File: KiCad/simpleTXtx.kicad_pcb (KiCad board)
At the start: 2 copper layers, 18 x 30 mm, 13 parts, among them J1 BAT, J2 VIDEO, Q1 2SC1815

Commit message: update project
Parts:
- removed J1: BAT, Connector_PinHeader_2.54mm:PinHeader_1x02_P2.54mm_Vertical
- added J3: RCJ-044, RCJ-044:CUI_RCJ-044, F.Cu at (157.0, 85.0)
- C3, C4: footprint Capacitor_THT:C_Disc_D4.3mm_W1.9mm_P5.00mm -> Capacitor_THT:C_Disc_D11.0mm_W5.0mm_P5.00mm
- J2: value VIDEO -> Barrel_Jack_MountingPin; footprint Connector_PinHeader_2.54mm:PinHeader_1x02_P2.54mm_Vertical -> Connector_BarrelJack:BarrelJack_GCT_DCJ200-10-A_Horizontal
- RV1: footprint Potentiometer_THT:Potentiometer_Bourns_3266Y_Vertical -> Potentiometer_THT:Potentiometer_Runtron_RM-065_Vertical
- moved J2 22.1 mm to (138.5, 75.7), turned to 0 degrees
- moved C5 19.9 mm to (155.0, 59.0)
- moved RV1 18.1 mm to (134.5, 59.5)
- moved C4 16.4 mm to (136.0, 69.5), turned to 0 degrees
- moved L1 13.0 mm to (148.0, 79.7), turned to -90 degrees
- moved C3 4.41 mm to (148.0, 68.4), turned to -90 degrees
- moved AE1 4.01 mm to (147.0, 60.5)
- moved C2 2.28 mm to (157.0, 70.5)
- moved R1 2.16 mm to (160.5, 67.5)
- moved C1 2.14 mm to (160.5, 70.5)
- moved R2 1.19 mm to (153.5, 70.5)
- moved Q1 1.04 mm to (154.0, 66.5)
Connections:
- C5 pad 2: Net-(J2-Pad1) -> Net-(C5-Pad2)
- J2 pad 1: Net-(J2-Pad1) -> Net-(C1-Pad2)
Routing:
- net Net-(C5-Pad2): track 0.00 -> 20.8 mm
- net Net-(AE1-A): track 18.8 -> 35.2 mm
- net Net-(J2-Pad1): track 12.5 -> 0.00 mm
- net Net-(Q1-C): track 30.8 -> 36.1 mm
- net GND: track 63.8 -> 62.4 mm
- net Net-(C1-Pad2): track 31.2 -> 31.7 mm
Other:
- board size 18 x 30 mm -> 30.5 x 33 mm
- board text removed: "9-12v"
- board text removed: "Antenna"
- board text removed: "GND"
- board text removed: "VIDEO"

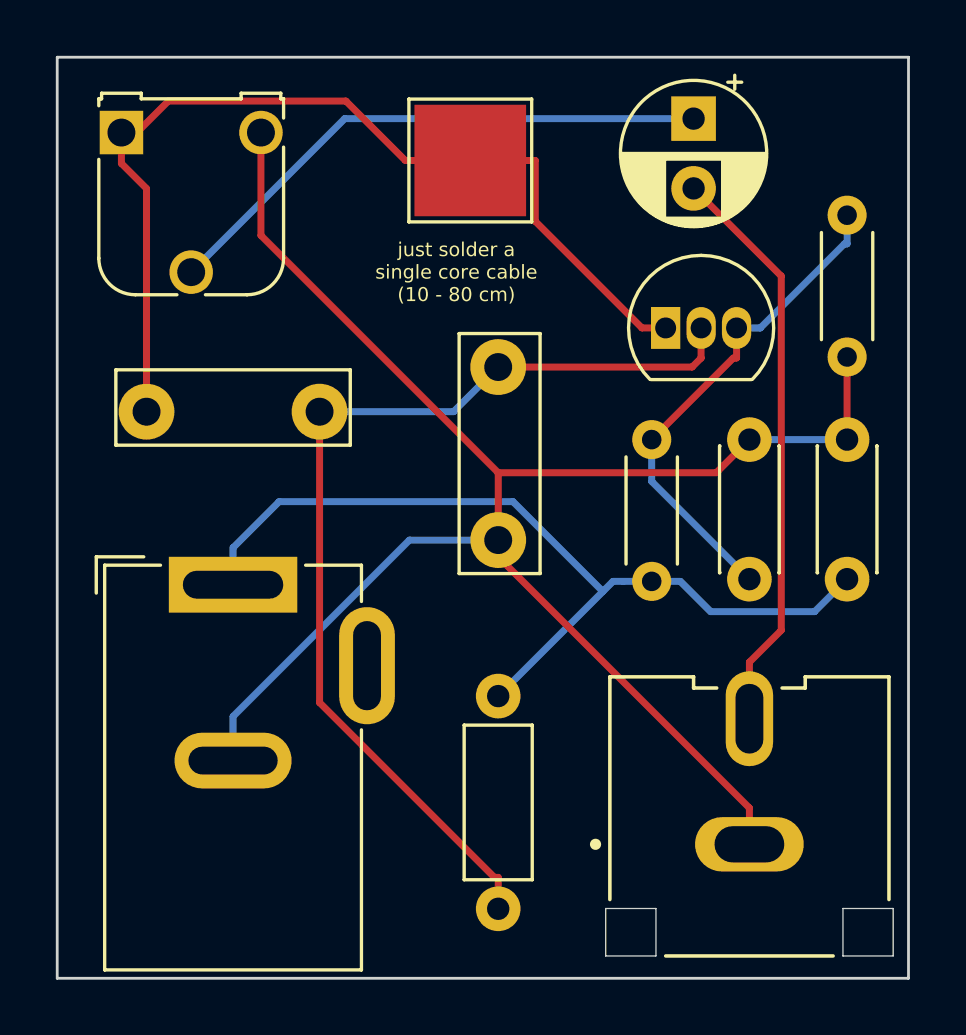
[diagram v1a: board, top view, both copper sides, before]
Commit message: remove one trimmer
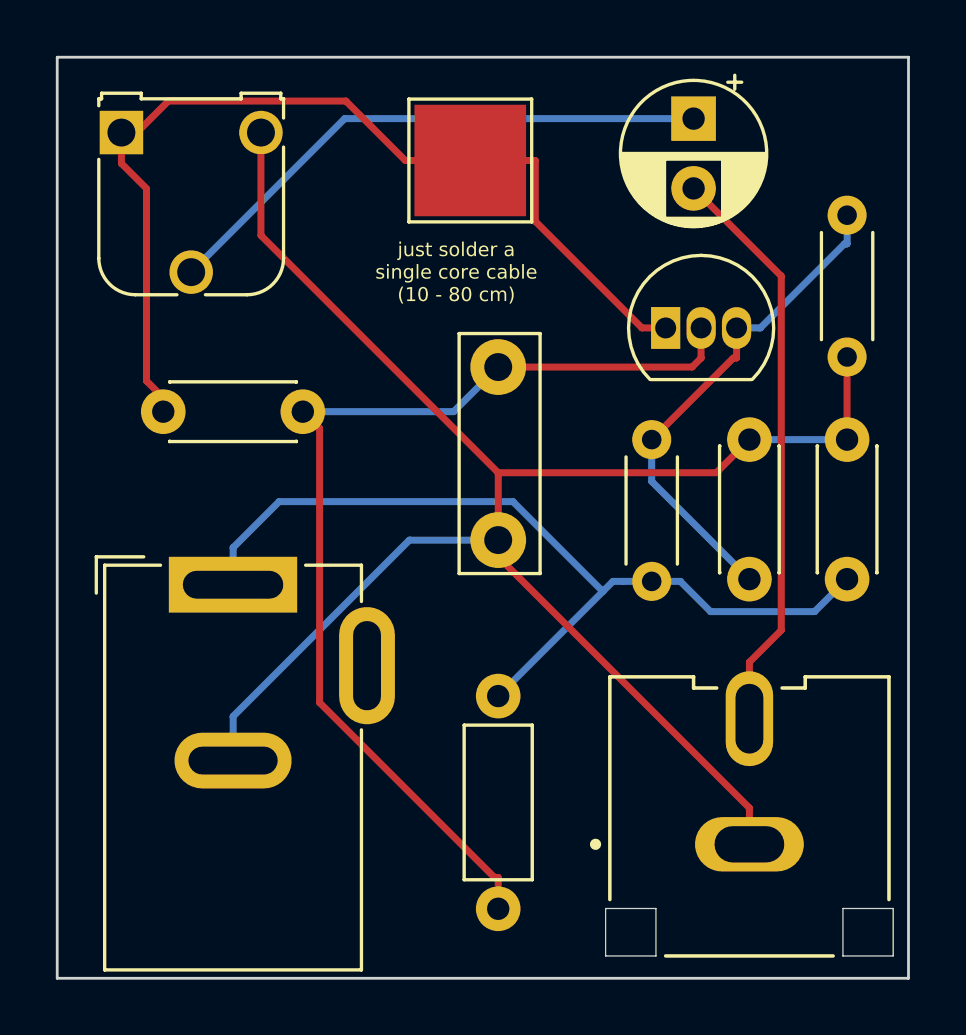
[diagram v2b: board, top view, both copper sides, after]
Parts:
- removed C4: 10pF, Capacitor_THT:C_Disc_D11.0mm_W5.0mm_P5.00mm
- added C6: 10pF, Capacitor_THT:C_Disc_D4.3mm_W1.9mm_P5.00mm, F.Cu at (136.0, 69.5)
- J2: value Barrel_Jack_MountingPin -> power
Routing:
- net Net-(Q1-C): track 36.1 -> 36.9 mm
